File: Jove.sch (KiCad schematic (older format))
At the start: 153 parts, among them J1 PJ301B, J2 PJ301B, J3 PJ301B, J4 PJ301B, J5 PJ301B, J6 PJ301B, P1 CONN_02X05, Q1 BCM857BS, Q2 BCM857BS, Q3 J112, Q4 J112, Q5 J112, Q6 J112, SW1 KS-01Q, U1 TL072-, U10 CD4027, U11 CD40106, U12 TS321, U13 TS321, U2 TL072-, U3 TL072-, U4 TL072-, U5 LM13700, U6 LM13700, U7 LM13700, U8 DG409, U9 CD4052

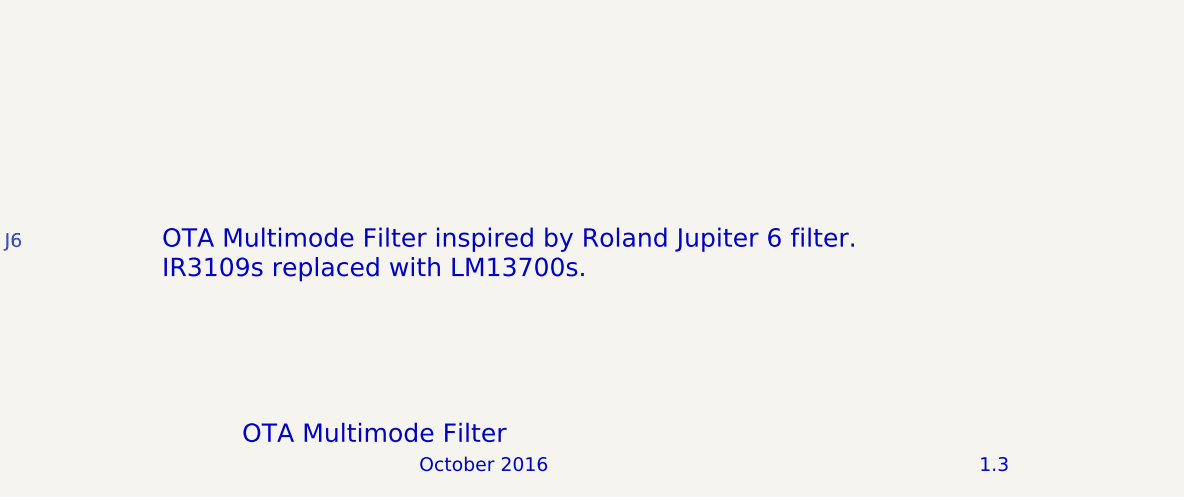
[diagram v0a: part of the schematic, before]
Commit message: rename project files to Jove
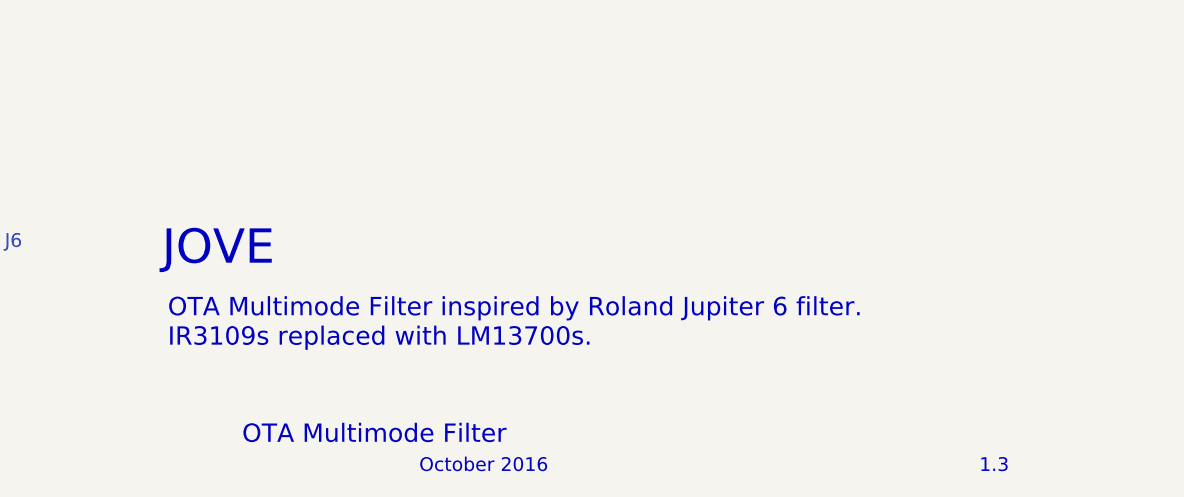
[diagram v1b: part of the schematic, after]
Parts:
- C23, C24: Part Number (none) -> UWJ1E100MCL1GB
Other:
- note added: "JOVE"
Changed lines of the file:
@@
 F 2 "Capacitors_SMD:c_elec_5x5.3" H 17750 1900 60  0001 C CNN
 F 3 "" H 17750 1900 60  0000 C CNN
+F 4 "UWJ1E100MCL1GB" H 17750 1900 60  0001 C CNN "Part Number"
 	1    17750 1900
 	1    0    0    -1
@@
 F 2 "Capacitors_SMD:c_elec_5x5.3" H 17750 2400 60  0001 C CNN
 F 3 "" H 17750 2400 60  0000 C CNN
+F 4 "UWJ1E100MCL1GB" H 17750 2400 60  0001 C CNN "Part Number"
 	1    17750 2400
 	1    0    0    -1
@@
 	3825 5200 4250 5200
 Connection ~ 4250 5525
-Text Notes 17300 15525 0    80   ~ 0
+Text Notes 17325 15825 0    80   ~ 0
 OTA Multimode Filter inspired by Roland Jupiter 6 filter. \nIR3109s replaced with LM13700s.
 Wire Wire Line
 	4000 1700 4125 1700
+Text Notes 17300 15475 0    150  ~ 0
+JOVE
 $EndSCHEMATC

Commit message: updated rescue library references to new project name
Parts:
- Q3, Q4, Q5, Q6: symbol Q_NJFET_SDG-RESCUE-Eurorack-JP6-filter -> Q_NJFET_SDG-RESCUE-Jove
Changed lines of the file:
@@
 EESchema Schematic File Version 2
-LIBS:Eurorack-JP6-filter-rescue
+LIBS:Jove-rescue
 LIBS:MySynthParts
 LIBS:device
@@
 LIBS:contrib
 LIBS:valves
-LIBS:Eurorack-JP6-filter-cache
+LIBS:Jove-cache
 EELAYER 25 0
 EELAYER END
@@
 NoConn ~ 15850 15450
 $Comp
-L Q_NJFET_SDG-RESCUE-Eurorack-JP6-filter Q6
+L Q_NJFET_SDG-RESCUE-Jove Q6
 U 1 1 554F0331
 P 19425 11775
@@
 $EndComp
 $Comp
-L Q_NJFET_SDG-RESCUE-Eurorack-JP6-filter Q5
+L Q_NJFET_SDG-RESCUE-Jove Q5
 U 1 1 554F0714
 P 16825 11775
@@
 $EndComp
 $Comp
-L Q_NJFET_SDG-RESCUE-Eurorack-JP6-filter Q4
+L Q_NJFET_SDG-RESCUE-Jove Q4
 U 1 1 554F0CB3
 P 11125 11775
@@
 $EndComp
 $Comp
-L Q_NJFET_SDG-RESCUE-Eurorack-JP6-filter Q3
+L Q_NJFET_SDG-RESCUE-Jove Q3
 U 1 1 554F15DD
 P 8525 11775

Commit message: genereated gerbers for panelization by PCB house
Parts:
- Q3, Q4, Q5, Q6: symbol Q_NJFET_SDG-RESCUE-Jove -> Q_NJFET_SDG
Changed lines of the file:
@@
 NoConn ~ 15850 15450
 $Comp
-L Q_NJFET_SDG-RESCUE-Jove Q6
+L Q_NJFET_SDG Q6
 U 1 1 554F0331
 P 19425 11775
@@
 $EndComp
 $Comp
-L Q_NJFET_SDG-RESCUE-Jove Q5
+L Q_NJFET_SDG Q5
 U 1 1 554F0714
 P 16825 11775
@@
 $EndComp
 $Comp
-L Q_NJFET_SDG-RESCUE-Jove Q4
+L Q_NJFET_SDG Q4
 U 1 1 554F0CB3
 P 11125 11775
@@
 $EndComp
 $Comp
-L Q_NJFET_SDG-RESCUE-Jove Q3
+L Q_NJFET_SDG Q3
 U 1 1 554F15DD
 P 8525 11775

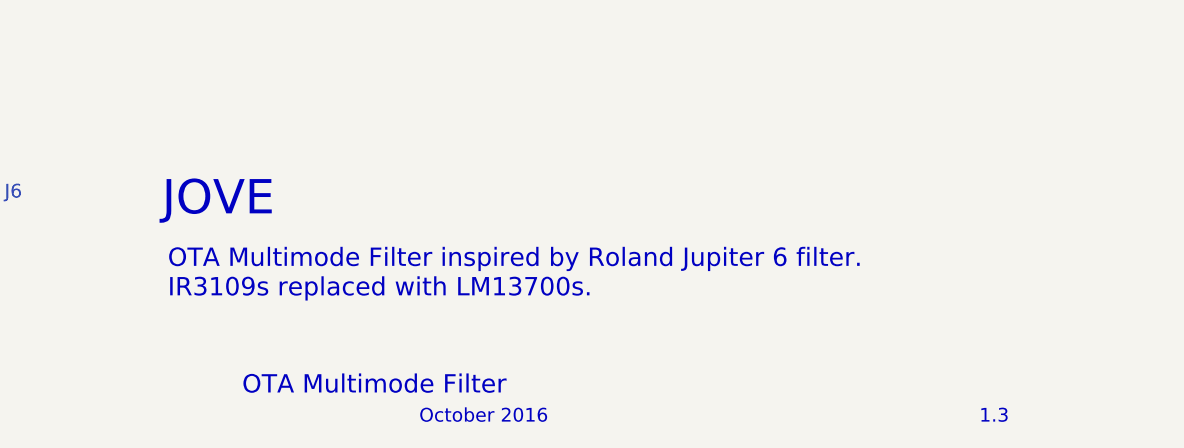
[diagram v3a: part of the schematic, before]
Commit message: corrected D6/D7 reference swap on PCB. Started working on manual
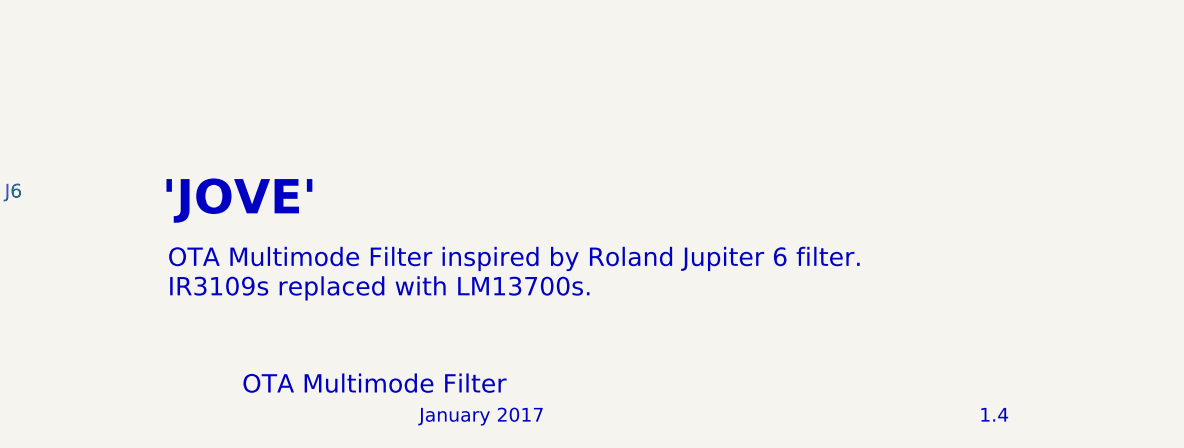
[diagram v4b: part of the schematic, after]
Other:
- note added: "'JOVE'"
- note added: "1.4"
- note added: "January 2017"
- note removed: "1.3"
- note removed: "JOVE"
- note removed: "October 2016"
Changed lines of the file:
@@
 OTA Multimode Filter
 Text Notes 20875 16375 0    60   ~ 0
-1.3
+1.4
 Text Notes 16200 15200 0    60   ~ 0
 OUT
 Text Notes 18425 16375 0    60   ~ 0
-October 2016
+January 2017
 $Comp
 L C_US C29
@@
 Wire Wire Line
 	4000 1700 4125 1700
-Text Notes 17300 15475 0    150  ~ 0
-JOVE
+Text Notes 17300 15475 0    150  ~ 30
+'JOVE'
 $EndSCHEMATC

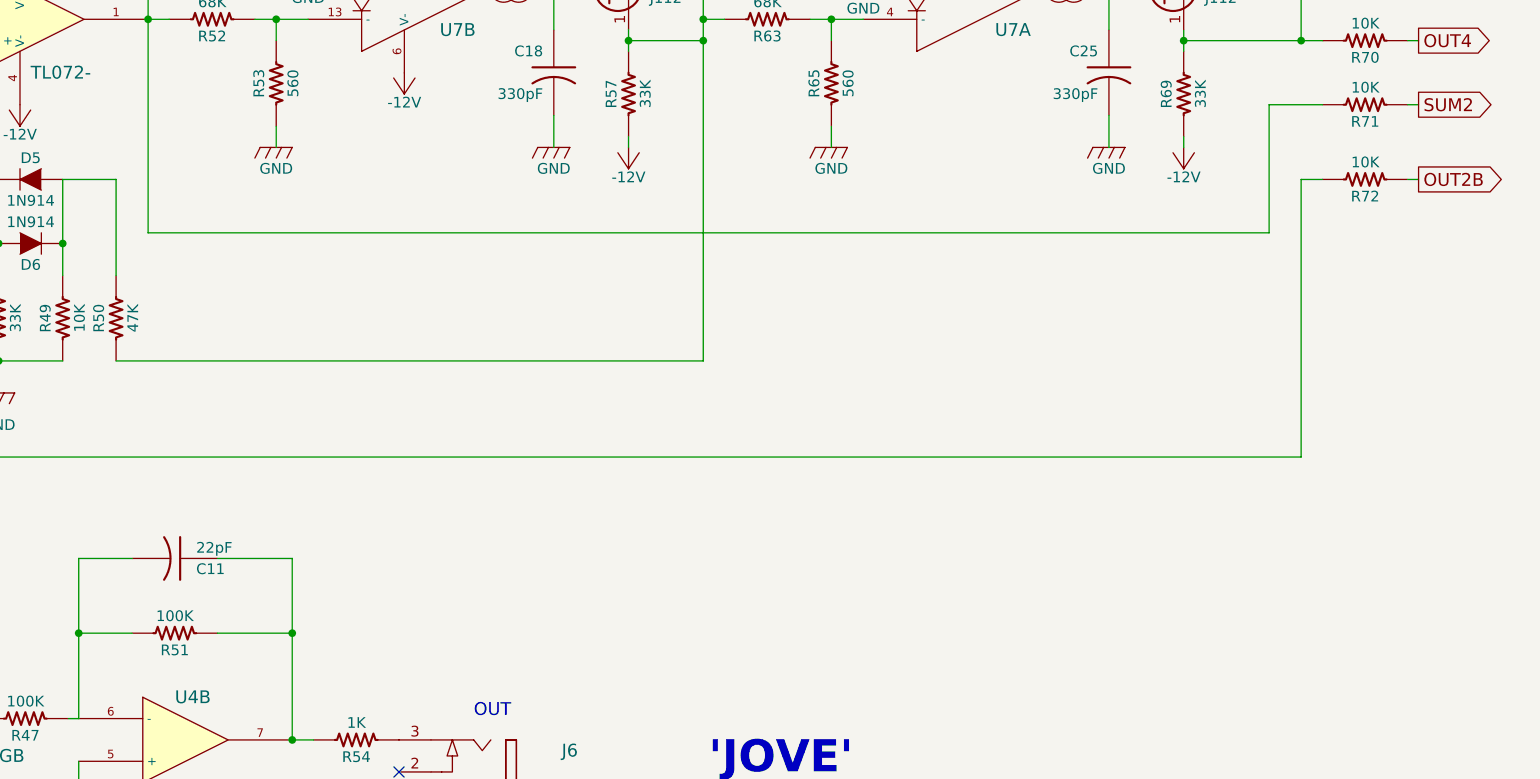
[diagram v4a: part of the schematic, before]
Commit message: changed R51 and R72 values to incrase overall output gain and bring down LP12 output levels to match other modes
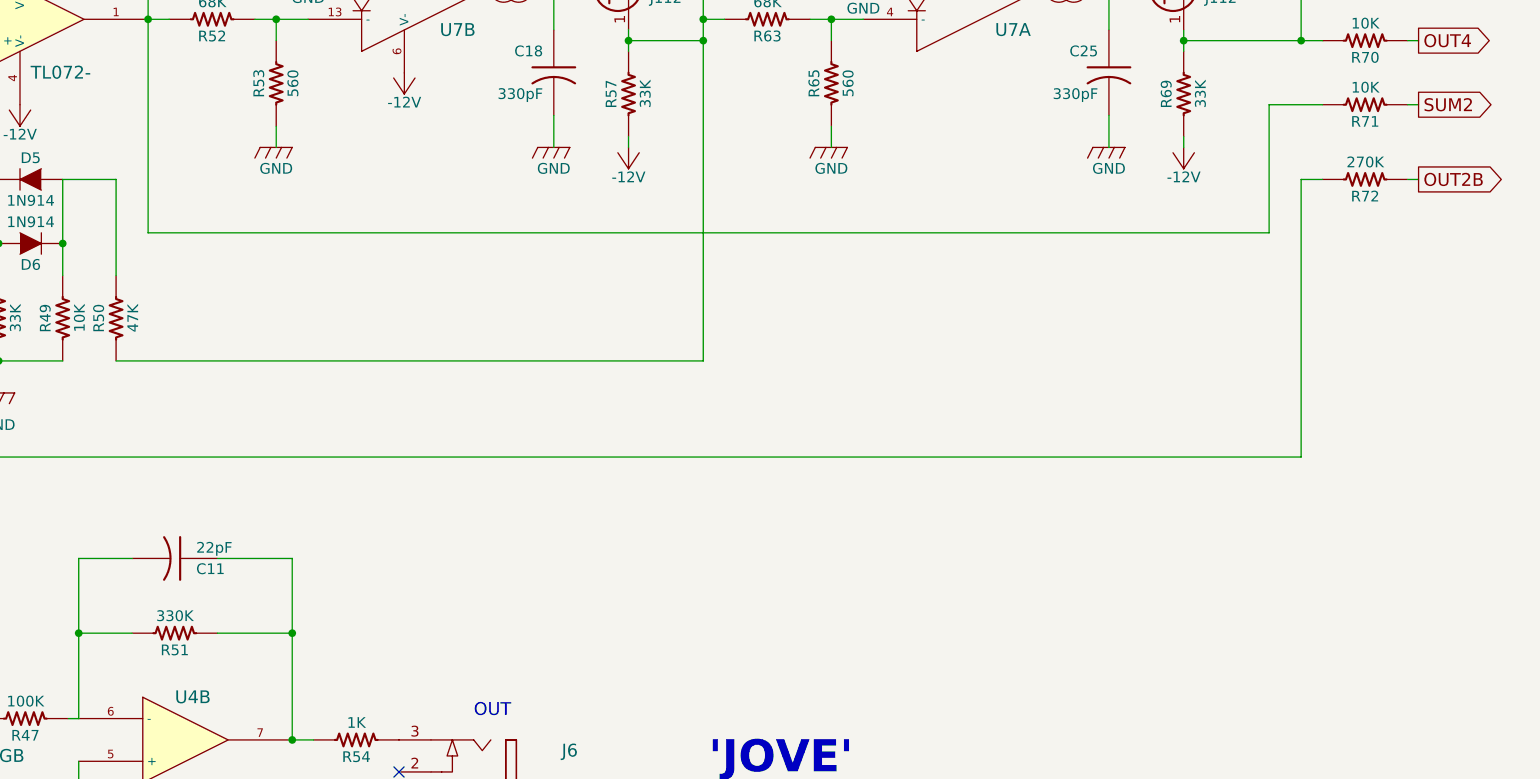
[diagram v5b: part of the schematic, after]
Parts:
- R51: value 100K -> 330K
- R72: value 10K -> 270K
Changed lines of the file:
@@
 P 20375 12675
 F 0 "R72" V 20455 12675 50  0000 C CNN
-F 1 "10K" V 20295 12675 50  0000 C CNN
+F 1 "270K" V 20295 12675 50  0000 C CNN
 F 2 "MyModules:SM0603-R-JRL" H 20375 12675 60  0001 C CNN
 F 3 "" H 20375 12675 60  0000 C CNN
@@
 P 14800 14800
 F 0 "R51" V 14880 14800 50  0000 C CNN
-F 1 "100K" V 14720 14800 50  0000 C CNN
+F 1 "330K" V 14720 14800 50  0000 C CNN
 F 2 "MyModules:SM0603-R-JRL" H 14800 14800 60  0001 C CNN
 F 3 "" H 14800 14800 60  0000 C CNN

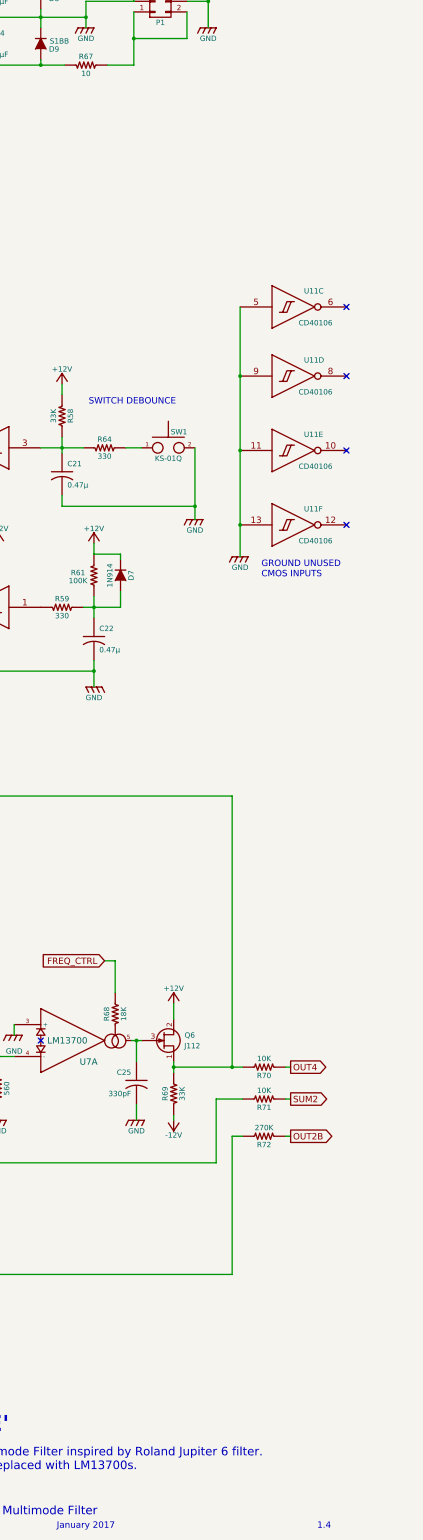
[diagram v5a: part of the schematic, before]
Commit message: updated BOM, readme, added octopart link
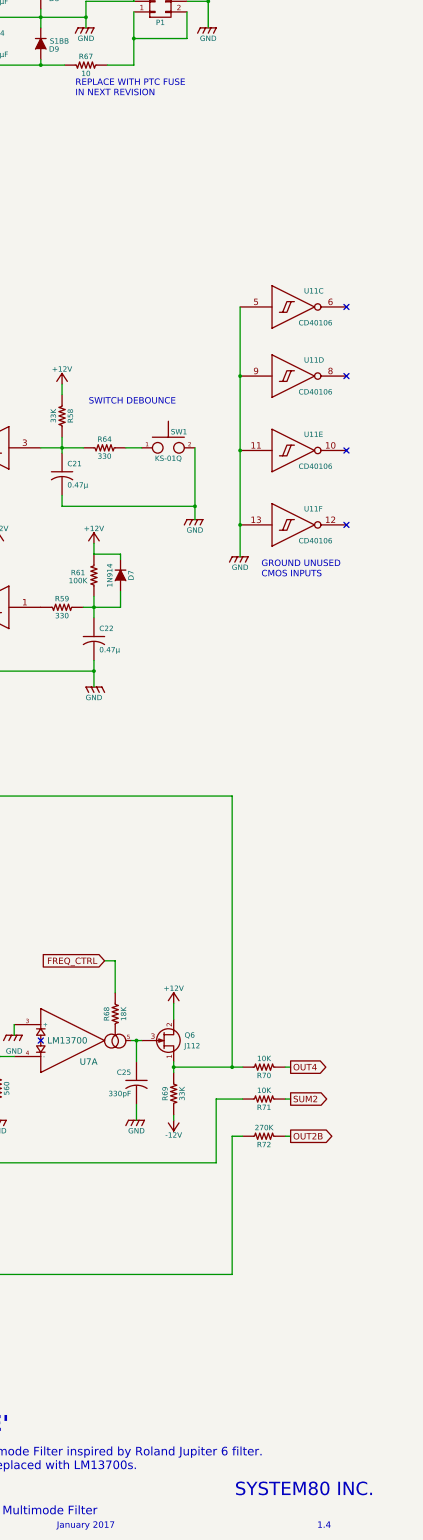
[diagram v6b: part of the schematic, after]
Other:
- note added: "REPLACE WITH PTC FUSE \nIN NEXT REVISION"
- note added: "SYSTEM80 INC."
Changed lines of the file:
@@
 Text Notes 17300 15475 0    150  ~ 30
 'JOVE'
+Text Notes 20100 16075 0    125  ~ 0
+SYSTEM80 INC.
+Text Notes 18600 2900 0    60   ~ 0
+REPLACE WITH PTC FUSE \nIN NEXT REVISION
 $EndSCHEMATC
